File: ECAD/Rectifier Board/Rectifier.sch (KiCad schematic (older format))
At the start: 3 parts

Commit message: rectifier
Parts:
- added C? (x3): 1uF, symbol Device:C
- added C?: 1000uF, symbol Device:CP
- added R?: 11K, symbol Device:R
- added R?: 1K, symbol Device:R
- added U?: LM317_TO-220, Package_TO_SOT_THT:TO-220-3_Vertical, symbol Regulator_Linear:LM317_TO-220
- D?: value D_Bridge_+-AA -> FULL BRIDGE
- J?: value 40VAC -> 30VAC
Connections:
- net labels added: +15V
- wire segments 9 -> 26
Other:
- moved on the sheet: U?
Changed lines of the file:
@@
 P 3000 2950
 F 0 "D?" H 3344 2996 50  0000 L CNN
-F 1 "D_Bridge_+-AA" H 3344 2905 50  0000 L CNN
+F 1 "FULL BRIDGE" H 3344 2905 50  0000 L CNN
 F 2 "" H 3000 2950 50  0001 C CNN
 F 3 "~" H 3000 2950 50  0001 C CNN
@@
 L Regulator_Controller:IR1153S U?
 U 1 1 62058102
-P 4800 4150
-F 0 "U?" H 4800 4831 50  0000 C CNN
-F 1 "IR1153S" H 4800 4740 50  0000 C CNN
-F 2 "Package_SO:SOIC-8_3.9x4.9mm_P1.27mm" H 4800 4150 50  0001 C CIN
-F 3 "https://www.infineon.com/dgdl/ir1153.pdf?fileId=5546d462533600a4015355c42a5b1649" H 4800 4150 50  0001 C CNN
-	1    4800 4150
+P 6400 4450
+F 0 "U?" H 6450 5000 50  0000 L CNN
+F 1 "IR1153S" H 6450 4900 50  0000 L CNN
+F 2 "Package_SO:SOIC-8_3.9x4.9mm_P1.27mm" H 6400 4450 50  0001 C CIN
+F 3 "https://www.infineon.com/dgdl/ir1153.pdf?fileId=5546d462533600a4015355c42a5b1649" H 6400 4450 50  0001 C CNN
+	1    6400 4450
 	1    0    0    -1
 $EndComp
@@
 P 2150 3000
 F 0 "J?" H 2068 2675 50  0000 C CNN
-F 1 "40VAC" H 2068 2766 50  0000 C CNN
+F 1 "30VAC" H 2068 2766 50  0000 C CNN
 F 2 "" H 2150 3000 50  0001 C CNN
 F 3 "~" H 2150 3000 50  0001 C CNN
@@
 Wire Wire Line
 	2700 3500 3300 3500
-Wire Wire Line
-	3300 2950 3300 2650
 $Comp
 L power:VCC #PWR?
 U 1 1 6205AED4
-P 3300 2650
-F 0 "#PWR?" H 3300 2500 50  0001 C CNN
-F 1 "VCC" H 3315 2823 50  0000 C CNN
-F 2 "" H 3300 2650 50  0001 C CNN
-F 3 "" H 3300 2650 50  0001 C CNN
-	1    3300 2650
-	1    0    0    -1
-$EndComp
+P 3300 2600
+F 0 "#PWR?" H 3300 2450 50  0001 C CNN
+F 1 "VCC" H 3315 2773 50  0000 C CNN
+F 2 "" H 3300 2600 50  0001 C CNN
+F 3 "" H 3300 2600 50  0001 C CNN
+	1    3300 2600
+	1    0    0    -1
+$EndComp
+$Comp
+L Regulator_Linear:LM317_TO-220 U?
+U 1 1 6205D4E8
+P 5150 2900
+F 0 "U?" H 5150 3142 50  0000 C CNN
+F 1 "LM317_TO-220" H 5150 3051 50  0000 C CNN
+F 2 "Package_TO_SOT_THT:TO-220-3_Vertical" H 5150 3150 50  0001 C CIN
+F 3 "http://www.ti.com/lit/ds/symlink/lm317.pdf" H 5150 2900 50  0001 C CNN
+	1    5150 2900
+	1    0    0    -1
+$EndComp
+$Comp
+L Device:R R?
+U 1 1 6205E083
+P 5150 3350
+F 0 "R?" H 5200 3350 50  0000 L CNN
+F 1 "11K" V 5150 3350 50  0000 C CNN
+F 2 "" V 5080 3350 50  0001 C CNN
+F 3 "~" H 5150 3350 50  0001 C CNN
+	1    5150 3350
+	1    0    0    -1
+$EndComp
+$Comp
+L Device:R R?
+U 1 1 6205F378
+P 5600 3050
+F 0 "R?" H 5650 3050 50  0000 L CNN
+F 1 "1K" V 5600 3050 50  0000 C CNN
+F 2 "" V 5530 3050 50  0001 C CNN
+F 3 "~" H 5600 3050 50  0001 C CNN
+	1    5600 3050
+	1    0    0    -1
+$EndComp
+Wire Wire Line
+	5150 3200 5600 3200
+Connection ~ 5150 3200
+Wire Wire Line
+	5600 2900 5450 2900
+$Comp
+L Device:C C?
+U 1 1 6205FE8A
+P 5900 3050
+F 0 "C?" H 6015 3096 50  0000 L CNN
+F 1 "1uF" H 6015 3005 50  0000 L CNN
+F 2 "" H 5938 2900 50  0001 C CNN
+F 3 "~" H 5900 3050 50  0001 C CNN
+	1    5900 3050
+	1    0    0    -1
+$EndComp
+$Comp
+L Device:C C?
+U 1 1 620613FC
+P 5600 3350
+F 0 "C?" H 5715 3396 50  0000 L CNN
+F 1 "1uF" H 5715 3305 50  0000 L CNN
+F 2 "" H 5638 3200 50  0001 C CNN
+F 3 "~" H 5600 3350 50  0001 C CNN
+	1    5600 3350
+	1    0    0    -1
+$EndComp
+Connection ~ 5600 3200
+Wire Wire Line
+	5150 3500 5600 3500
+Wire Wire Line
+	5600 3500 5900 3500
+Wire Wire Line
+	5900 3500 5900 3200
+Connection ~ 5600 3500
+Wire Wire Line
+	5900 2900 5600 2900
+Connection ~ 5600 2900
+$Comp
+L Device:C C?
+U 1 1 620625CD
+P 4500 3050
+F 0 "C?" H 4615 3096 50  0000 L CNN
+F 1 "1uF" H 4615 3005 50  0000 L CNN
+F 2 "" H 4538 2900 50  0001 C CNN
+F 3 "~" H 4500 3050 50  0001 C CNN
+	1    4500 3050
+	1    0    0    -1
+$EndComp
+Wire Wire Line
+	4500 3500 4500 3200
+Wire Wire Line
+	4850 2900 4500 2900
+Wire Wire Line
+	4500 3500 5150 3500
+Connection ~ 5150 3500
+$Comp
+L Device:CP C?
+U 1 1 62063BAE
+P 3950 3000
+F 0 "C?" H 4068 3046 50  0000 L CNN
+F 1 "1000uF" H 4068 2955 50  0000 L CNN
+F 2 "" H 3988 2850 50  0001 C CNN
+F 3 "~" H 3950 3000 50  0001 C CNN
+	1    3950 3000
+	1    0    0    -1
+$EndComp
+Wire Wire Line
+	3300 2600 3950 2600
+Connection ~ 3300 2600
+Wire Wire Line
+	3300 3500 3950 3500
+Wire Wire Line
+	3950 3500 3950 3150
+Connection ~ 3300 3500
+Wire Wire Line
+	3950 2600 4500 2600
+Connection ~ 3950 2600
+Wire Wire Line
+	4500 2900 4500 2600
+Connection ~ 4500 2900
+Connection ~ 4500 2600
+Wire Wire Line
+	4500 2600 5900 2600
+Wire Wire Line
+	3950 2600 3950 2850
+Wire Wire Line
+	3300 2600 3300 2950
+Wire Wire Line
+	3950 3500 4500 3500
+Connection ~ 3950 3500
+Connection ~ 4500 3500
+$Comp
+L power:+15V #PWR?
+U 1 1 6206D11A
+P 5900 2900
+F 0 "#PWR?" H 5900 2750 50  0001 C CNN
+F 1 "+15V" H 5915 3073 50  0000 C CNN
+F 2 "" H 5900 2900 50  0001 C CNN
+F 3 "" H 5900 2900 50  0001 C CNN
+	1    5900 2900
+	1    0    0    -1
+$EndComp
+Connection ~ 5900 2900
+$Comp
+L power:+15V #PWR?
+U 1 1 6206D895
+P 6400 3950
+F 0 "#PWR?" H 6400 3800 50  0001 C CNN
+F 1 "+15V" H 6415 4123 50  0000 C CNN
+F 2 "" H 6400 3950 50  0001 C CNN
+F 3 "" H 6400 3950 50  0001 C CNN
+	1    6400 3950
+	1    0    0    -1
+$EndComp

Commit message: assign footprints
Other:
- moved on the sheet: U?
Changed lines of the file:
@@
 L Regulator_Controller:IR1153S U?
 U 1 1 62058102
-P 6400 4450
-F 0 "U?" H 6450 5000 50  0000 L CNN
-F 1 "IR1153S" H 6450 4900 50  0000 L CNN
-F 2 "Package_SO:SOIC-8_3.9x4.9mm_P1.27mm" H 6400 4450 50  0001 C CIN
-F 3 "https://www.infineon.com/dgdl/ir1153.pdf?fileId=5546d462533600a4015355c42a5b1649" H 6400 4450 50  0001 C CNN
-	1    6400 4450
+P 7400 4450
+F 0 "U?" H 7450 5000 50  0000 L CNN
+F 1 "IR1153S" H 7450 4900 50  0000 L CNN
+F 2 "Package_SO:SOIC-8_3.9x4.9mm_P1.27mm" H 7400 4450 50  0001 C CIN
+F 3 "https://www.infineon.com/dgdl/ir1153.pdf?fileId=5546d462533600a4015355c42a5b1649" H 7400 4450 50  0001 C CNN
+	1    7400 4450
 	1    0    0    -1
 $EndComp
@@
 L power:+15V #PWR?
 U 1 1 6206D895
-P 6400 3950
-F 0 "#PWR?" H 6400 3800 50  0001 C CNN
-F 1 "+15V" H 6415 4123 50  0000 C CNN
-F 2 "" H 6400 3950 50  0001 C CNN
-F 3 "" H 6400 3950 50  0001 C CNN
-	1    6400 3950
-	1    0    0    -1
-$EndComp
+P 7400 3950
+F 0 "#PWR?" H 7400 3800 50  0001 C CNN
+F 1 "+15V" H 7415 4123 50  0000 C CNN
+F 2 "" H 7400 3950 50  0001 C CNN
+F 3 "" H 7400 3950 50  0001 C CNN
+	1    7400 3950
+	1    0    0    -1
+$EndComp
+$Comp
+L power:GND #PWR?
+U 1 1 620A7987
+P 7400 4950
+F 0 "#PWR?" H 7400 4700 50  0001 C CNN
+F 1 "GND" H 7405 4777 50  0000 C CNN
+F 2 "" H 7400 4950 50  0001 C CNN
+F 3 "" H 7400 4950 50  0001 C CNN
+	1    7400 4950
+	1    0    0    -1
+$EndComp

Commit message: start routing
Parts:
- added L?: L, symbol Device:L
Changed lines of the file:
@@
 	1    0    0    -1
 $EndComp
+$Comp
+L Device:L L?
+U 1 1 620C462E
+P 6600 2600
+F 0 "L?" V 6790 2600 50  0000 C CNN
+F 1 "L" V 6699 2600 50  0000 C CNN
+F 2 "" H 6600 2600 50  0001 C CNN
+F 3 "~" H 6600 2600 50  0001 C CNN
+	1    6600 2600
+	0    -1   -1   0
+$EndComp
 $EndSCHEMATC

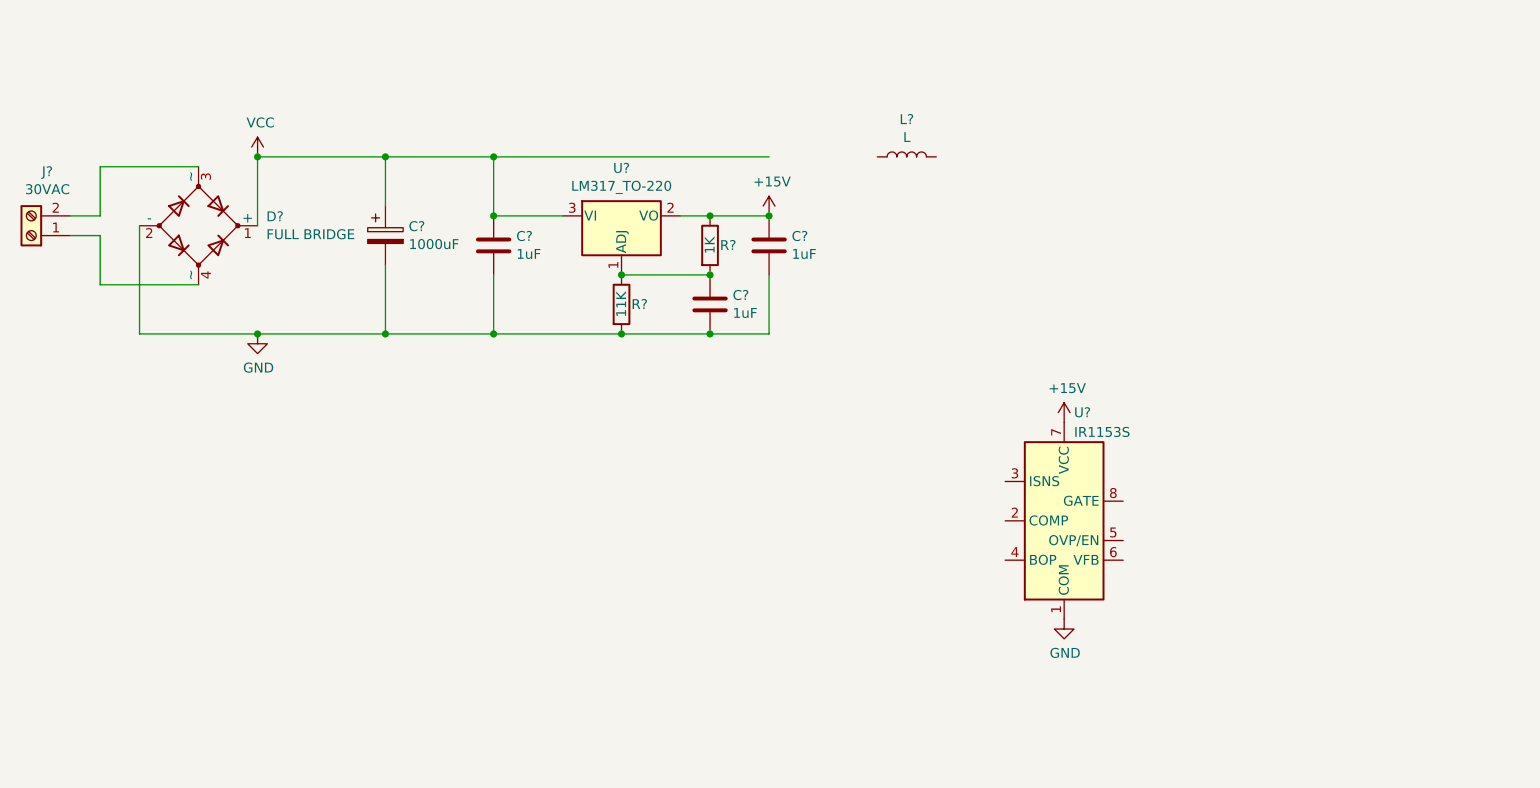
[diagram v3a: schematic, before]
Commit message: add apfc components
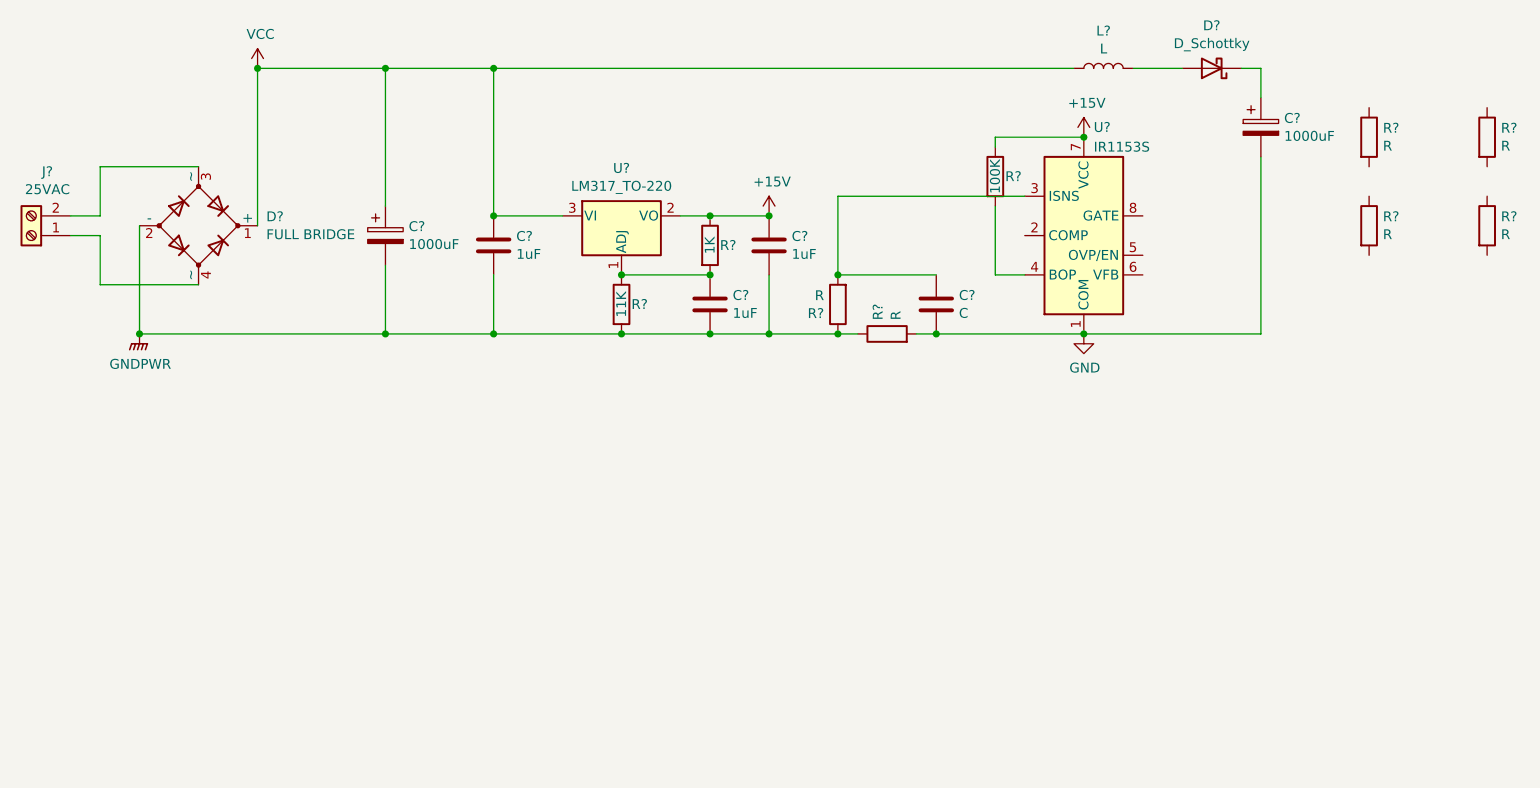
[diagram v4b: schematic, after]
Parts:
- added C?: 1000uF, symbol Device:CP
- added C?: C, symbol Device:C
- added D?: D_Schottky, symbol Device:D_Schottky
- added R? (x6): R, symbol Device:R
- added R?: 100K, symbol Device:R
- J?: value 30VAC -> 25VAC
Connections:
- net labels added: GNDPWR
- wire segments 26 -> 41
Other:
- moved on the sheet: L?, U?

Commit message: Cin
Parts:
- added C?: 10uF, symbol Device:CP
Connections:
- net GNDPWR: now also C?.2
- net VCC: now also C?.1
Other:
- moved on the sheet: C?, R?, U?
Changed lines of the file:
@@
 L Regulator_Linear:LM317_TO-220 U?
 U 1 1 6205D4E8
-P 5150 2900
-F 0 "U?" H 5150 3142 50  0000 C CNN
-F 1 "LM317_TO-220" H 5150 3051 50  0000 C CNN
-F 2 "Package_TO_SOT_THT:TO-220-3_Vertical" H 5150 3150 50  0001 C CIN
-F 3 "http://www.ti.com/lit/ds/symlink/lm317.pdf" H 5150 2900 50  0001 C CNN
-	1    5150 2900
+P 5050 2900
+F 0 "U?" H 5050 3142 50  0000 C CNN
+F 1 "LM317_TO-220" H 5050 3051 50  0000 C CNN
+F 2 "Package_TO_SOT_THT:TO-220-3_Vertical" H 5050 3150 50  0001 C CIN
+F 3 "http://www.ti.com/lit/ds/symlink/lm317.pdf" H 5050 2900 50  0001 C CNN
+	1    5050 2900
 	1    0    0    -1
 $EndComp
@@
 L Device:R R?
 U 1 1 6205E083
-P 5150 3350
-F 0 "R?" H 5200 3350 50  0000 L CNN
-F 1 "11K" V 5150 3350 50  0000 C CNN
-F 2 "" V 5080 3350 50  0001 C CNN
-F 3 "~" H 5150 3350 50  0001 C CNN
-	1    5150 3350
+P 5050 3350
+F 0 "R?" H 5100 3350 50  0000 L CNN
+F 1 "11K" V 5050 3350 50  0000 C CNN
+F 2 "" V 4980 3350 50  0001 C CNN
+F 3 "~" H 5050 3350 50  0001 C CNN
+	1    5050 3350
 	1    0    0    -1
 $EndComp
@@
 L Device:R R?
 U 1 1 6205F378
-P 5600 3050
-F 0 "R?" H 5650 3050 50  0000 L CNN
-F 1 "1K" V 5600 3050 50  0000 C CNN
-F 2 "" V 5530 3050 50  0001 C CNN
-F 3 "~" H 5600 3050 50  0001 C CNN
-	1    5600 3050
-	1    0    0    -1
-$EndComp
-Wire Wire Line
-	5150 3200 5600 3200
-Connection ~ 5150 3200
-Wire Wire Line
-	5600 2900 5450 2900
+P 5500 3050
+F 0 "R?" H 5550 3050 50  0000 L CNN
+F 1 "1K" V 5500 3050 50  0000 C CNN
+F 2 "" V 5430 3050 50  0001 C CNN
+F 3 "~" H 5500 3050 50  0001 C CNN
+	1    5500 3050
+	1    0    0    -1
+$EndComp
+Wire Wire Line
+	5050 3200 5500 3200
+Connection ~ 5050 3200
+Wire Wire Line
+	5500 2900 5350 2900
 $Comp
 L Device:C C?
 U 1 1 6205FE8A
-P 5900 3050
-F 0 "C?" H 6015 3096 50  0000 L CNN
-F 1 "1uF" H 6015 3005 50  0000 L CNN
-F 2 "" H 5938 2900 50  0001 C CNN
-F 3 "~" H 5900 3050 50  0001 C CNN
-	1    5900 3050
+P 5800 3050
+F 0 "C?" H 5915 3096 50  0000 L CNN
+F 1 "1uF" H 5915 3005 50  0000 L CNN
+F 2 "" H 5838 2900 50  0001 C CNN
+F 3 "~" H 5800 3050 50  0001 C CNN
+	1    5800 3050
 	1    0    0    -1
 $EndComp
@@
 L Device:C C?
 U 1 1 620613FC
-P 5600 3350
-F 0 "C?" H 5715 3396 50  0000 L CNN
-F 1 "1uF" H 5715 3305 50  0000 L CNN
-F 2 "" H 5638 3200 50  0001 C CNN
-F 3 "~" H 5600 3350 50  0001 C CNN
-	1    5600 3350
-	1    0    0    -1
-$EndComp
-Connection ~ 5600 3200
-Wire Wire Line
-	5150 3500 5600 3500
-Wire Wire Line
-	5600 3500 5900 3500
-Wire Wire Line
-	5900 3500 5900 3200
-Connection ~ 5600 3500
-Wire Wire Line
-	5900 2900 5600 2900
-Connection ~ 5600 2900
+P 5500 3350
+F 0 "C?" H 5615 3396 50  0000 L CNN
+F 1 "1uF" H 5615 3305 50  0000 L CNN
+F 2 "" H 5538 3200 50  0001 C CNN
+F 3 "~" H 5500 3350 50  0001 C CNN
+	1    5500 3350
+	1    0    0    -1
+$EndComp
+Connection ~ 5500 3200
+Wire Wire Line
+	5800 3500 5800 3200
+Wire Wire Line
+	5800 2900 5500 2900
+Connection ~ 5500 2900
 $Comp
 L Device:C C?
 U 1 1 620625CD
-P 4500 3050
-F 0 "C?" H 4615 3096 50  0000 L CNN
-F 1 "1uF" H 4615 3005 50  0000 L CNN
-F 2 "" H 4538 2900 50  0001 C CNN
-F 3 "~" H 4500 3050 50  0001 C CNN
-	1    4500 3050
-	1    0    0    -1
-$EndComp
-Wire Wire Line
-	4500 3500 4500 3200
-Wire Wire Line
-	4850 2900 4500 2900
-Wire Wire Line
-	4500 3500 5150 3500
-Connection ~ 5150 3500
+P 4400 3050
+F 0 "C?" H 4515 3096 50  0000 L CNN
+F 1 "1uF" H 4515 3005 50  0000 L CNN
+F 2 "" H 4438 2900 50  0001 C CNN
+F 3 "~" H 4400 3050 50  0001 C CNN
+	1    4400 3050
+	1    0    0    -1
+$EndComp
+Wire Wire Line
+	4400 3500 4400 3200
+Wire Wire Line
+	4750 2900 4400 2900
 $Comp
 L Device:CP C?
@@
 	3950 3500 3950 3150
 Wire Wire Line
-	3950 2150 4500 2150
+	3950 2150 4400 2150
 Connection ~ 3950 2150
-Connection ~ 4500 2150
-Wire Wire Line
-	3950 3500 4500 3500
+Wire Wire Line
+	3950 3500 4400 3500
 Connection ~ 3950 3500
-Connection ~ 4500 3500
 $Comp
 L power:+15V #PWR?
 U 1 1 6206D11A
-P 5900 2900
-F 0 "#PWR?" H 5900 2750 50  0001 C CNN
-F 1 "+15V" H 5915 3073 50  0000 C CNN
-F 2 "" H 5900 2900 50  0001 C CNN
-F 3 "" H 5900 2900 50  0001 C CNN
-	1    5900 2900
-	1    0    0    -1
-$EndComp
-Connection ~ 5900 2900
+P 5800 2900
+F 0 "#PWR?" H 5800 2750 50  0001 C CNN
+F 1 "+15V" H 5815 3073 50  0000 C CNN
+F 2 "" H 5800 2900 50  0001 C CNN
+F 3 "" H 5800 2900 50  0001 C CNN
+	1    5800 2900
+	1    0    0    -1
+$EndComp
+Connection ~ 5800 2900
 $Comp
 L power:+15V #PWR?
@@
 Wire Wire Line
 	6250 3500 6350 3500
-Wire Wire Line
-	6250 3500 5900 3500
 Connection ~ 6250 3500
-Connection ~ 5900 3500
 Wire Wire Line
 	6650 3500 6750 3500
 Wire Wire Line
-	4500 2150 4500 2900
-Connection ~ 4500 2900
+	4400 2150 4400 2900
+Connection ~ 4400 2900
 Wire Wire Line
 	3950 2150 3950 2850
@@
 	7050 3200 7200 3200
 Wire Wire Line
-	4500 2150 7450 2150
-Wire Wire Line
 	8400 2300 8400 2150
 Wire Wire Line
@@
 Wire Wire Line
 	8400 3500 7500 3500
+Connection ~ 4400 2150
+Connection ~ 4400 3500
+Connection ~ 5050 3500
+Connection ~ 5500 3500
+Connection ~ 5800 3500
+Wire Wire Line
+	5050 3500 5500 3500
+Wire Wire Line
+	5500 3500 5800 3500
+Wire Wire Line
+	4400 3500 5050 3500
+Wire Wire Line
+	5800 3500 6050 3500
+$Comp
+L Device:CP C?
+U 1 1 621098C4
+P 6050 2450
+F 0 "C?" H 6168 2496 50  0000 L CNN
+F 1 "10uF" H 6168 2405 50  0000 L CNN
+F 2 "" H 6088 2300 50  0001 C CNN
+F 3 "~" H 6050 2450 50  0001 C CNN
+	1    6050 2450
+	1    0    0    -1
+$EndComp
+Wire Wire Line
+	4400 2150 6050 2150
+Wire Wire Line
+	6050 2300 6050 2150
+Connection ~ 6050 2150
+Wire Wire Line
+	6050 2150 7450 2150
+Wire Wire Line
+	6050 2600 6050 3500
+Connection ~ 6050 3500
+Wire Wire Line
+	6050 3500 6250 3500
 $EndSCHEMATC

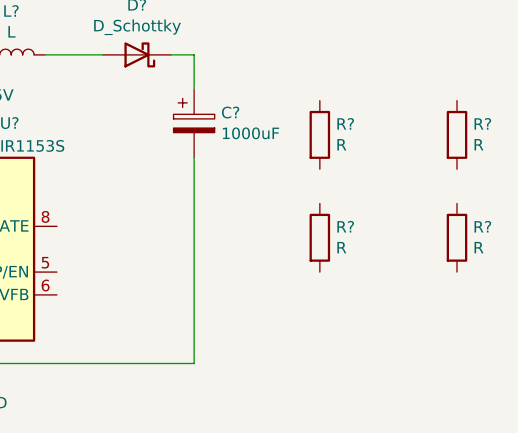
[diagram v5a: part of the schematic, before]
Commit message: Begin to replace LM317 with switching regulator
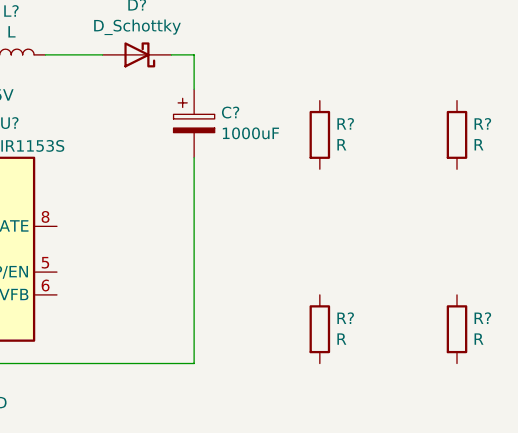
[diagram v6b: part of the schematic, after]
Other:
- moved on the sheet: R?
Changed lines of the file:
@@
 L Device:R R?
 U 1 1 621099B6
-P 8950 2950
-F 0 "R?" H 9020 2996 50  0000 L CNN
-F 1 "R" H 9020 2905 50  0000 L CNN
-F 2 "" V 8880 2950 50  0001 C CNN
-F 3 "~" H 8950 2950 50  0001 C CNN
-	1    8950 2950
+P 8950 3350
+F 0 "R?" H 9020 3396 50  0000 L CNN
+F 1 "R" H 9020 3305 50  0000 L CNN
+F 2 "" V 8880 3350 50  0001 C CNN
+F 3 "~" H 8950 3350 50  0001 C CNN
+	1    8950 3350
 	1    0    0    -1
 $EndComp
@@
 L Device:R R?
 U 1 1 6210AF08
-P 9550 2950
-F 0 "R?" H 9620 2996 50  0000 L CNN
-F 1 "R" H 9620 2905 50  0000 L CNN
-F 2 "" V 9480 2950 50  0001 C CNN
-F 3 "~" H 9550 2950 50  0001 C CNN
-	1    9550 2950
+P 9550 3350
+F 0 "R?" H 9620 3396 50  0000 L CNN
+F 1 "R" H 9620 3305 50  0000 L CNN
+F 2 "" V 9480 3350 50  0001 C CNN
+F 3 "~" H 9550 3350 50  0001 C CNN
+	1    9550 3350
 	1    0    0    -1
 $EndComp
